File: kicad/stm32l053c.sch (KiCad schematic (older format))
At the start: 43 parts, among them J1 GND, J10 3V3, J11 I2C, J2 GND, J3 TX, J4 GND, J5 TEST_1P, J6 TEST_1P, J8 RX, P1 SWD, U1 AP2112, U2 STM32L053C8_LQFP48, U3 ADS1015, U4 UFL_SMA, U5 RFM92/95

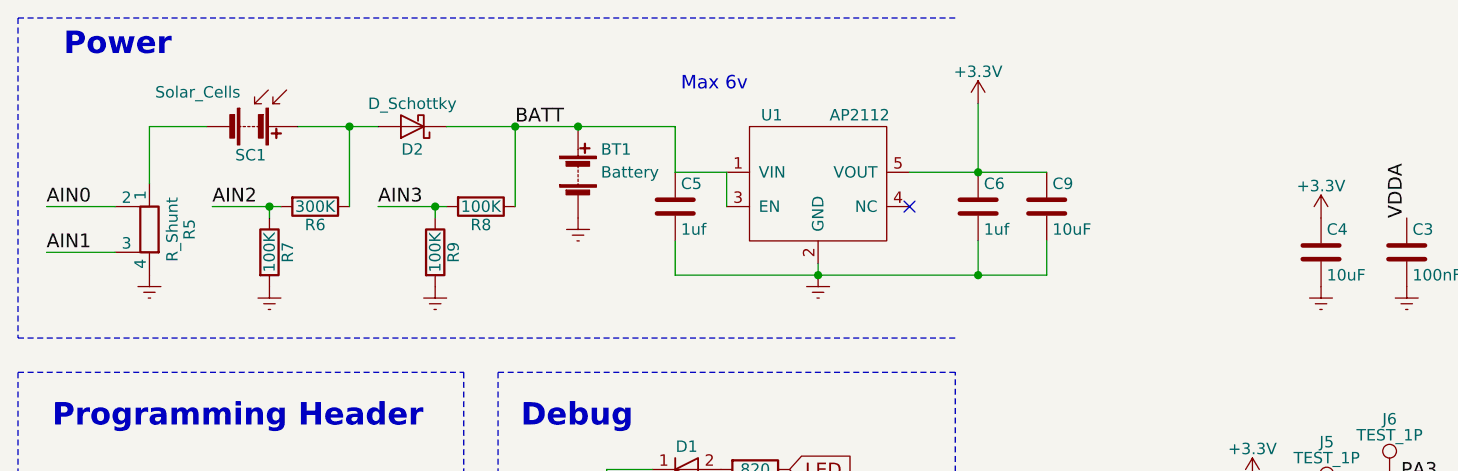
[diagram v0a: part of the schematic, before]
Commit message: Off board regulator & off board shunt
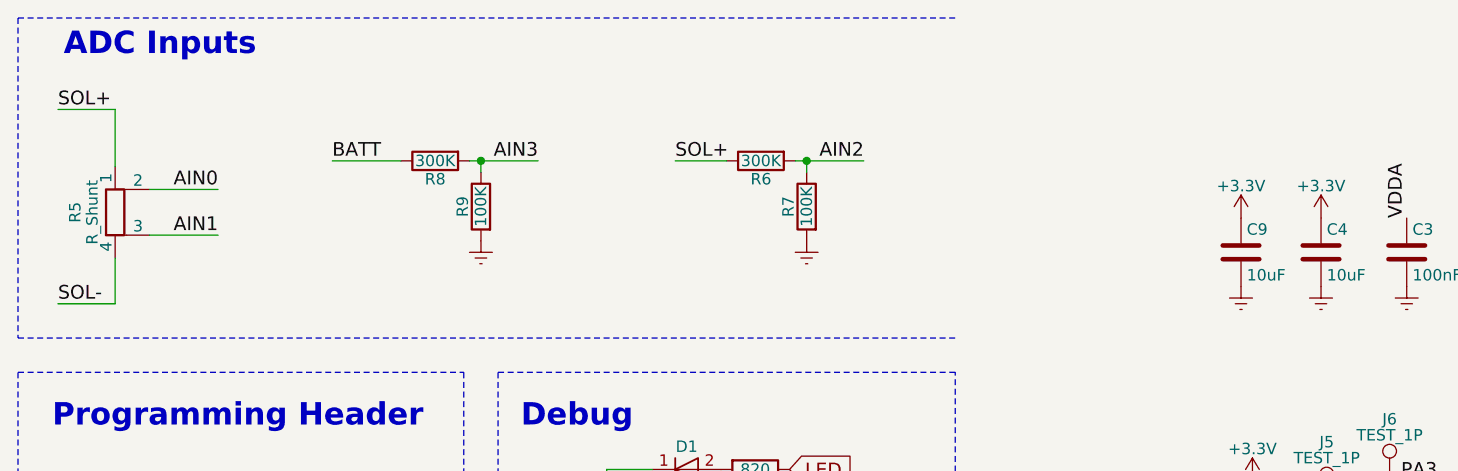
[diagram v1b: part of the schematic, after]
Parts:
- removed BT1: Battery, theapi:BatteryBoxAndPins, symbol Battery
- removed C5, C6: 1uf, Capacitors_SMD:C_0805_HandSoldering, symbol C
- removed D2: D_Schottky, theapi:D_SOD-323_HandSoldering, symbol D_Schottky
- removed SC1: Solar_Cells, Pin_Headers:Pin_Header_Straight_1x02_Pitch2.54mm, symbol Solar_Cells
- removed U1: AP2112, TO_SOT_Packages_SMD:SOT-23-5_HandSoldering, symbol AP2112
- R8: value 100K -> 300K
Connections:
- net Earth: no longer R5.4
- net SOL+: now reaches R6.1
- net SOL+: now also R5.1
- new net SOL-: R5.4
- no-connect marks 12 -> 11
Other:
- note added: "ADC Inputs"
- note removed: "Max 6v"
- note removed: "Power"
- moved on the sheet: C9, R5, R6, R7, R8, R9
